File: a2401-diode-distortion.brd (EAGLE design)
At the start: 100 x 80 mm, 39 parts, among them U1 FX2-20P-1.27DS, U2 FX2-20S-1.27DS

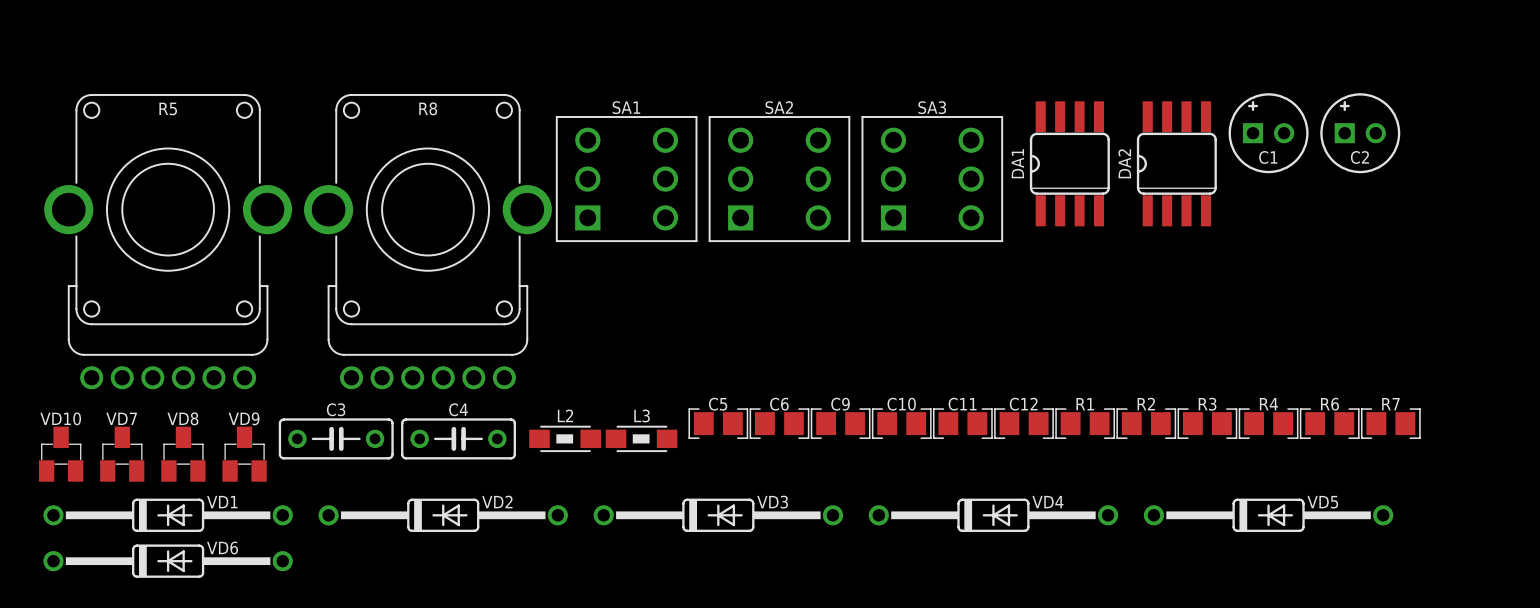
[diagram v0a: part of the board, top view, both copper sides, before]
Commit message: Replaced bypass switch with blend potentiometer
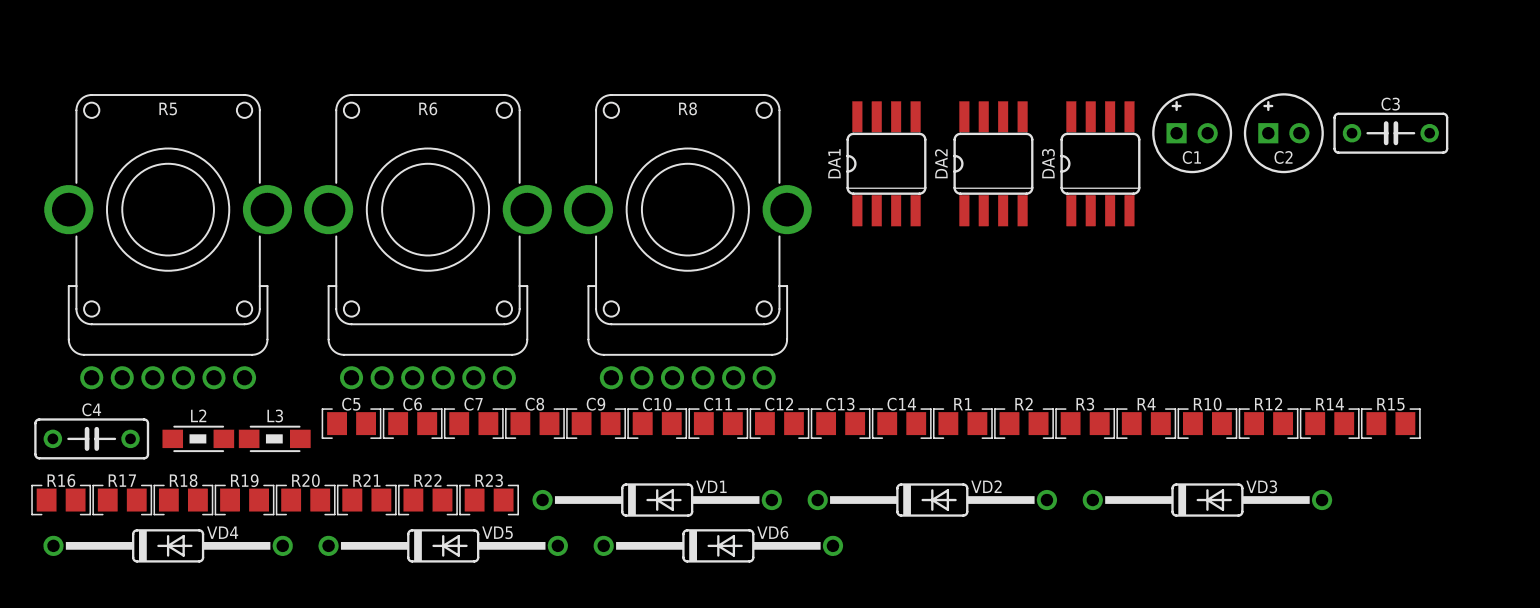
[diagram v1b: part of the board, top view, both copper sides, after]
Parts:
- removed SA1, SA2, SA3: 108-0052-EVX, switches:108-0052-EVX
- removed VD10, VD7, VD8, VD9: BAV199, diodes:SOT23
- added C13, C14: 100N, capacitors:C-0805
- added C7, C8: 22P, capacitors:C-0805
- added DA3: NJM2068M, ic-jrc:SO-8
- added R10, R12, R14, R16, R17, R18, R19, R20, R21: 10K, resistors:R-0805
- added R22, R23: 15K, resistors:R-0805
- R15: value 100K -> 10K
- R6: value 100K -> 2*B20K(CD); device resistors:R-0805 -> potentiometers:RV11-DUAL
- moved C3 71.8 mm to (89.0, -64.0)
- moved R6 60.6 mm to (26.0, -69.0)
- moved VD4 54.0 mm to (9.00, -91.0)
- moved VD5 54.0 mm to (27.0, -91.0)
- moved O1 36.0 mm to (55.0, -91.0)
- moved U1 36.0 mm to (58.0, -91.0)
- moved U2 36.0 mm to (61.0, -91.0)
- moved VD6 36.0 mm to (45.0, -91.0)
- moved VD1 32.0 mm to (41.0, -88.0)
- moved VD2 32.0 mm to (59.0, -88.0)
- moved VD3 32.0 mm to (77.0, -88.0)
- moved C4 24.0 mm to (4.00, -84.0)
- moved C5 24.0 mm to (21.0, -83.0)
- moved C6 24.0 mm to (25.0, -83.0)
- moved L2 24.0 mm to (11.0, -84.0)
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- renumbered R7 to R15
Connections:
- removed net N$21: SA3.6, VD2.A, VD5.C
- removed net N$22: SA1.5, SA3.5, VD10.2, VD9.1
- removed net N$25: PCB1.BOUTR', R15.1, SA2.5
- removed net N$28: PCB1.BOUTL', R6.1, SA2.2
- new net N$11: C8.1, DA3.6, R16.2, R23.1
- new net N$13: DA3.3, R19.2, R20.2
- new net N$15: R12.2, R14.1, R6.1'
- new net N$50: R18.2, R19.1, R6.1
- new net N$59: R10.2, R15.1, R6.3'
- new net N$64: C7.1, DA3.2, R21.2, R22.1
- new net N$7: C6.2, DA1.7, R5.2', R5.3', R8.3', VD2.C, VD6.A
- new net N$9: C5.2, DA1.1, R5.2, R5.3, R8.3, VD1.C, VD4.A
- net +15V: now also C13.2, DA3.8
- net -15V: now also C14.1, DA3.4
- net GND: now also C13.1, C14.2, R16.1, R21.1, R6.2'; no longer R15.2, SA1.3, SA1.6
- net N$10: now also VD2.A, VD5.C; no longer SA1.4
- net N$12: now also DA3.5, R14.2, R15.2; no longer C5.2, DA1.1, R5.2, R5.3, R8.3, VD1.C, VD4.A, VD7.2, VD7.3, VD8.1
- net N$17: now also C3.2, C5.1, DA1.2, R3.1; no longer SA3.3
- net N$18: now also DA1.3, PCB1.BINL, R17.1; no longer SA1.2, SA3.2, VD7.1, VD8.2
- net N$19: now also C8.2, DA3.7, PCB1.BOUTR', R23.2; no longer C6.2, DA1.7, R5.2', R5.3', R8.3', VD10.1, VD2.C, VD6.A, VD9.2, VD9.3
- net N$24: now also R12.1; no longer SA2.6
- net N$27: now also R18.1; no longer SA2.3
- net N$3: now also C7.2, DA3.1, PCB1.BOUTL', R22.2; no longer DA1.3, PCB1.BINL, SA2.1
- net N$5: now also R17.2, R20.1, R6.3; no longer C3.2, C5.1, DA1.2, R3.1, SA1.1
- net N$6: now also R10.1; no longer SA2.4

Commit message: a2401 diode distortion board
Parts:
- added O2, O3, O4: 450-AA150(15MM,D,BLACK), hardware:EMPTY
- added O5: 450-CP155(15MM,GRAY/WHITE), hardware:EMPTY
- added O6: 450-CP157(15MM,WHITE/BLACK), hardware:EMPTY
- added O7: 450-CP153(15MM,BLUE/WHITE), hardware:EMPTY
- C10, C11, C12, C13, C14, C9: value 100N -> 100N(TH); device capacitors:C-0805 -> capacitors:C050-024X044
- C5, C6, C7, C8: value 22P -> 22P(TH); device capacitors:C-0805 -> capacitors:C050-024X044
- DA1, DA3: value NJM2068M -> NE5532P; device ic-jrc:SO-8 -> ic-ti:DIP-8
- DA2: value NJM5532M -> TL072IP; device ic-jrc:SO-8 -> ic-ti:DIP-8
- L2, L3: value BLM31AJ601SN1L -> BL01RN1A1F1J; device inductors:1206 -> inductors:BL01RN1A
- R1, R2: value 4K7 -> 4K7(TH); device resistors:R-0805 -> resistors:R-0207/10
- R10, R12, R14, R15, R16, R17, R18, R19, R20, R21: value 10K -> 10K(TH); device resistors:R-0805 -> resistors:R-0207/10
- R22, R23: value 15K -> 15K(TH); device resistors:R-0805 -> resistors:R-0207/10
- R3, R4: value 33K -> 33K(TH); device resistors:R-0805 -> resistors:R-0207/10
- moved C4 145.4 mm to (72.0, 44.5), turned to 180 degrees
- moved R15 141.5 mm to (19.0, 40.0)
- moved R14 137.4 mm to (19.0, 37.5)
- moved R12 133.3 mm to (19.0, 35.0), turned to 180 degrees
- moved R16 129.0 mm to (32.0, 37.5)
- moved C2 129.0 mm to (10.0, 43.0)
- moved L3 126.0 mm to (32.0, 41.0), turned to 180 degrees
- moved R2 124.6 mm to (69.0, 41.5)
- moved VD5 124.1 mm to (50.0, 31.0), turned to 180 degrees
- moved R23 123.0 mm to (32.0, 35.0), turned to 180 degrees
- moved VD2 121.8 mm to (50.0, 33.5)
- moved VD4 119.7 mm to (50.0, 21.5)
- moved VD6 119.6 mm to (50.0, 28.5)
- moved C6 117.4 mm to (71.0, 25.0), turned to 180 degrees
- moved C10 116.4 mm to (62.0, 31.5), turned to 90 degrees
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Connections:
- net N$23: now also R8.2; no longer R8.2'
- net N$26: now also R8.2'; no longer R8.2
- net N$7: now also R8.3; no longer R8.3'
- net N$9: now also R8.3'; no longer R8.3
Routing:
- net -15V: track 0.00 -> 113.4 mm, vias 0 -> 2
- net N$7: track 0.00 -> 99.6 mm
- net +15V: track 0.00 -> 97.5 mm, vias 0 -> 2
- net N$9: track 0.00 -> 94.3 mm, vias 0 -> 1
- net N$6: track 0.00 -> 62.8 mm, vias 0 -> 2
- net N$18: track 0.00 -> 62.4 mm
- net N$24: track 0.00 -> 62.4 mm
- net N$10: track 0.00 -> 55.3 mm
- net N$27: track 0.00 -> 53.5 mm, vias 0 -> 1
- net N$16: track 0.00 -> 52.3 mm
- net N$3: track 0.00 -> 50.7 mm, vias 0 -> 1
- net N$17: track 0.00 -> 48.0 mm
- net P+15V: track 0.00 -> 45.9 mm
- net N$19: track 0.00 -> 44.9 mm
- net N$36: track 0.00 -> 43.4 mm
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- added copper zone on layer 1, net GND
- added copper zone on layer 16, net GND
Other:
- board size 100 x 80 mm -> 100 x 50 mm
